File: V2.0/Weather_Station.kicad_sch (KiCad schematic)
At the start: 41 parts, among them J1 HS91L02W2C01, J2 TYPE-C16PIN, J3 B-2100S04P-A110, J4 B-2100S04P-A110, J5 ZX-PZ2.54-1-6PZZ, U1 STM32F103C8T6, U2 HDC1080DMBR, U3 AMS1117-3.3, U5 SRV05-4, Y1 X322516MLB4SI

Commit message: Progressed with much more cleaner design.
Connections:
- net LED_B: now also U1.13 (PA3); no longer U1.2 (PC13)
- net LED_R: now also U1.20 (PB2); no longer U1.3 (PC14)
- net LED_W: now also U1.17 (PA7); no longer U1.4 (PC15)
- net RTC_CLK: now also U1.41 (PB5); no longer U1.18 (PB0)
- net RTC_INT: now also U1.40 (PB4); no longer U1.19 (PB1)
- net Shield: now reaches J2.S1 (SHIELD), R9.2
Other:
- moved on the sheet: R9
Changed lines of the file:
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@@
 	)
 	(no_connect
-		(at 114.3 99.06)
-	)
-	(no_connect
 		(at 146.05 210.82)
 	)
 	(no_connect
-		(at 114.3 106.68)
-	)
-	(no_connect
 		(at 114.3 114.3)
 	)
@@
 	)
 	(no_connect
-		(at 147.32 73.66)
+		(at 114.3 86.36)
 	)
 	(no_connect
@@
 	)
 	(no_connect
-		(at 114.3 104.14)
-	)
-	(no_connect
-		(at 147.32 83.82)
+		(at 114.3 93.98)
 	)
 	(no_connect
@@
 	)
 	(no_connect
+		(at 114.3 83.82)
+	)
+	(no_connect
 		(at 147.32 99.06)
 	)
@@
 	)
 	(no_connect
+		(at 114.3 88.9)
+	)
+	(no_connect
 		(at 146.05 205.74)
 	)
@@
 		(at 146.05 203.2)
 	)
+	(no_connect
+		(at 114.3 96.52)
+	)
 	(wire
 		(pts
@@
 	(wire
 		(pts
-			(xy 111.76 88.9) (xy 114.3 88.9)
+			(xy 88.9 111.76) (xy 114.3 111.76)
 		)
 		(stroke
@@
 	(wire
 		(pts
-			(xy 88.9 111.76) (xy 114.3 111.76)
+			(xy 147.32 93.98) (xy 148.59 93.98)
 		)
 		(stroke
@@
 	(wire
 		(pts
-			(xy 147.32 93.98) (xy 148.59 93.98)
+			(xy 111.76 106.68) (xy 114.3 106.68)
 		)
 		(stroke
@@
 	(wire
 		(pts
+			(xy 361.95 80.01) (xy 361.95 76.2)
+		)
+		(stroke
+			(width 0)
+			(type default)
+		)
+	)
+	(wire
+		(pts
 			(xy 52.07 90.17) (xy 59.69 90.17)
 		)
@@
 	(wire
 		(pts
-			(xy 111.76 83.82) (xy 114.3 83.82)
+			(xy 111.76 99.06) (xy 114.3 99.06)
 		)
 		(stroke
@@
 	(wire
 		(pts
-			(xy 111.76 93.98) (xy 114.3 93.98)
-		)
-		(stroke
-			(width 0)
-			(type default)
-		)
-	)
-	(wire
-		(pts
 			(xy 58.42 36.83) (xy 76.2 36.83)
 		)
@@
 	(wire
 		(pts
-			(xy 111.76 96.52) (xy 114.3 96.52)
-		)
-		(stroke
-			(width 0)
-			(type default)
-		)
-	)
-	(wire
-		(pts
 			(xy 127 58.42) (xy 129.54 58.42)
 		)
@@
 	(wire
 		(pts
+			(xy 147.32 73.66) (xy 149.86 73.66)
+		)
+		(stroke
+			(width 0)
+			(type default)
+		)
+	)
+	(wire
+		(pts
 			(xy 73.66 71.12) (xy 73.66 69.85)
 		)
@@
 	(wire
 		(pts
+			(xy 354.33 80.01) (xy 361.95 80.01)
+		)
+		(stroke
+			(width 0)
+			(type default)
+		)
+	)
+	(wire
+		(pts
 			(xy 190.5 99.06) (xy 190.5 96.52)
 		)
@@
 	(wire
 		(pts
+			(xy 147.32 83.82) (xy 149.86 83.82)
+		)
+		(stroke
+			(width 0)
+			(type default)
+		)
+	)
+	(wire
+		(pts
 			(xy 52.07 104.14) (xy 59.69 104.14)
 		)
@@
 	(wire
 		(pts
-			(xy 129.54 140.97) (xy 132.08 140.97)
+			(xy 111.76 104.14) (xy 114.3 104.14)
 		)
 		(stroke
@@
 	(wire
 		(pts
-			(xy 129.54 58.42) (xy 132.08 58.42)
+			(xy 129.54 140.97) (xy 132.08 140.97)
 		)
 		(stroke
@@
 	(wire
 		(pts
-			(xy 73.66 209.55) (xy 83.82 209.55)
+			(xy 129.54 58.42) (xy 132.08 58.42)
 		)
 		(stroke
@@
 	(wire
 		(pts
-			(xy 332.74 80.01) (xy 354.33 80.01)
+			(xy 73.66 209.55) (xy 83.82 209.55)
 		)
 		(stroke
@@
 	(wire
 		(pts
-			(xy 300.99 24.13) (xy 328.93 24.13)
+			(xy 332.74 80.01) (xy 346.71 80.01)
 		)
 		(stroke
@@
 	(wire
 		(pts
-			(xy 59.69 104.14) (xy 59.69 101.6)
+			(xy 300.99 24.13) (xy 328.93 24.13)
 		)
 		(stroke
@@
 	(wire
 		(pts
-			(xy 88.9 95.25) (xy 88.9 96.52)
+			(xy 59.69 104.14) (xy 59.69 101.6)
 		)
 		(stroke
@@
 	(wire
 		(pts
-			(xy 58.42 46.99) (xy 76.2 46.99)
+			(xy 88.9 95.25) (xy 88.9 96.52)
 		)
 		(stroke
@@
 	(wire
 		(pts
-			(xy 111.76 86.36) (xy 114.3 86.36)
+			(xy 58.42 46.99) (xy 76.2 46.99)
 		)
 		(stroke
@@
 	(wire
 		(pts
-			(xy 361.95 80.01) (xy 361.95 76.2)
-		)
-		(stroke
-			(width 0)
-			(type default)
-		)
-	)
-	(wire
-		(pts
 			(xy 297.18 176.53) (xy 309.88 176.53)
 		)
@@
 	)
 	(label "LED_B"
-		(at 111.76 83.82 180)
+		(at 149.86 73.66 0)
 		(fields_autoplaced yes)
 		(effects
@@
 				(size 1.27 1.27)
 			)
-			(justify right bottom)
+			(justify left bottom)
 		)
 	)
@@
 	)
 	(label "RTC_CLK"
-		(at 111.76 93.98 180)
+		(at 111.76 106.68 180)
 		(fields_autoplaced yes)
 		(effects
@@
 	)
 	(label "RTC_INT"
-		(at 111.76 96.52 180)
+		(at 111.76 104.14 180)
 		(fields_autoplaced yes)
 		(effects
@@
 	)
 	(label "LED_R"
-		(at 111.76 86.36 180)
+		(at 111.76 99.06 180)
 		(fields_autoplaced yes)
 		(effects
@@
 	)
 	(label "LED_W"
-		(at 111.76 88.9 180)
+		(at 149.86 83.82 0)
 		(fields_autoplaced yes)
 		(effects
@@
 				(size 1.27 1.27)
 			)
-			(justify right bottom)
+			(justify left bottom)
 		)
 	)
@@
 		)
 	)
+	(label "Shield"
+		(at 355.6 80.01 0)
+		(fields_autoplaced yes)
+		(effects
+			(font
+				(size 1.27 1.27)
+			)
+			(justify left bottom)
+		)
+	)
 	(symbol
 		(lib_id "power:GND")
@@
 	(symbol
 		(lib_id "Device:R")
-		(at 358.14 80.01 90)
+		(at 350.52 80.01 90)
 		(unit 1)
 		(exclude_from_sim no)
@@
 		(dnp no)
 		(property "Reference" "R9"
-			(at 358.14 83.82 90)
+			(at 350.52 83.82 90)
 			(effects
 				(font
@@
 		)
 		(property "Value" "1M"
-			(at 358.14 86.36 90)
+			(at 350.52 86.36 90)
 			(effects
 				(font
@@
 		)
 		(property "Footprint" "Resistor_SMD:R_0603_1608Metric"
-			(at 358.14 81.788 90)
+			(at 350.52 81.788 90)
 			(effects
 				(font
@@
 		)
 		(property "Datasheet" "~"
-			(at 358.14 80.01 0)
+			(at 350.52 80.01 0)
 			(effects
 				(font
@@
 		)
 		(property "Description" "Resistor"
-			(at 358.14 80.01 0)
+			(at 350.52 80.01 0)
 			(effects
 				(font

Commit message: This is ordered Version of Weather Station V2!!!
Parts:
- FB1: footprint Inductor_SMD:L_1206_3216Metric -> Inductor_SMD:L_0603_1608Metric
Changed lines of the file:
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@@
 			)
 		)
-		(property "Footprint" "Inductor_SMD:L_1206_3216Metric"
+		(property "Footprint" "Inductor_SMD:L_0603_1608Metric"
 			(at 173.99 38.608 90)
 			(effects

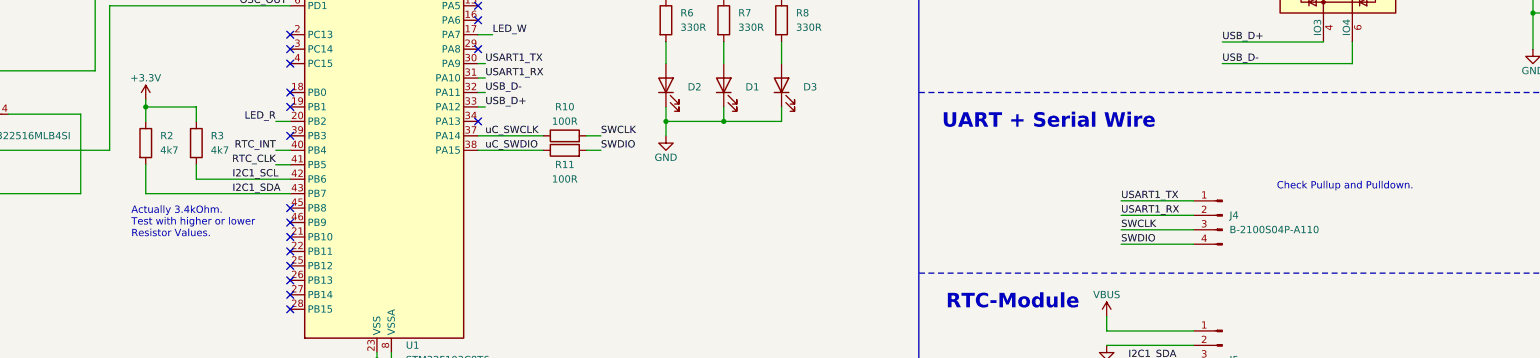
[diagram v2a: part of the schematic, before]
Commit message: Added ToDo for next Version.
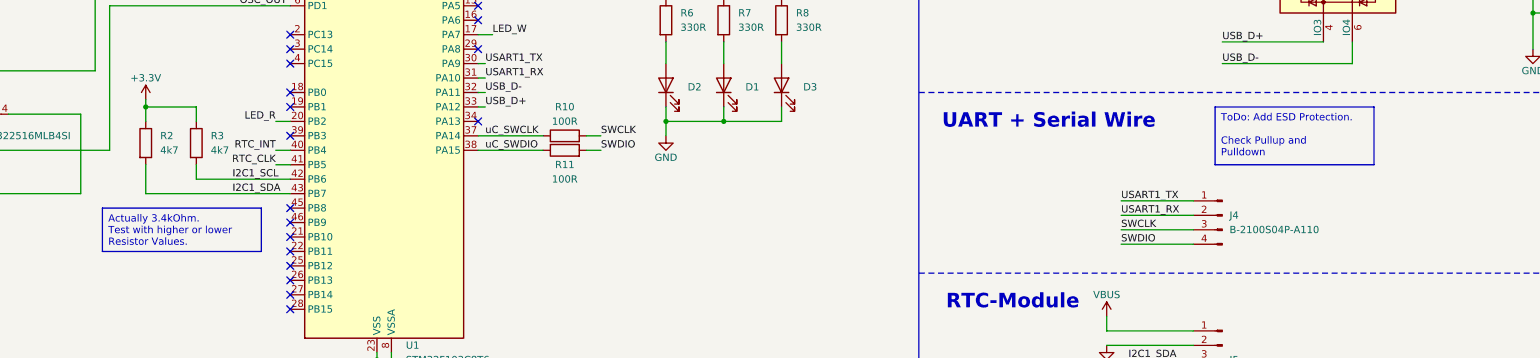
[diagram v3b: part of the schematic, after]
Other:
- note removed: "Actually 3.4kOhm. Test with higher or lower Resistor Values."
- note removed: "Check Pullup and Pulldown."
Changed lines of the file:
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@@
+		)
+	)
+	(text_box "Actually 3.4kOhm.\nTest with higher or lower \nResistor Values."
+		(exclude_from_sim no)
+		(at 81.28 114.3 0)
+		(size 27.94 7.62)
+		(stroke
+			(width 0)
+			(type default)
+		)
+		(fill
+			(type color)
+			(color 255 255 0 1)
+		)
+		(effects
+			(font
+				(size 1.27 1.27)
+			)
+			(justify left top)
+		)
+	)
+	(text_box "ToDo: Add ESD Protection.\n\nCheck Pullup and Pulldown"
+		(exclude_from_sim no)
+		(at 276.86 96.52 0)
+		(size 27.94 10.16)
+		(stroke
+			(width 0)
+			(type default)
+		)
+		(fill
+			(type color)
+			(color 255 255 0 1)
+		)
+		(effects
+			(font
+				(size 1.27 1.27)
+			)
+			(justify left top)
 		)
 	)
@@
 				(bold yes)
 			)
-		)
-	)
-	(text "Actually 3.4kOhm.\nTest with higher or lower \nResistor Values."
-		(exclude_from_sim no)
-		(at 86.36 116.84 0)
-		(effects
-			(font
-				(size 1.27 1.27)
-			)
-			(justify left)
 		)
 	)
@@
 			)
 		)
-	)
-	(text "Check Pullup and Pulldown."
-		(exclude_from_sim no)
-		(at 299.72 110.49 0)
-		(effects
-			(font
-				(size 1.27 1.27)
-			)
-		)
